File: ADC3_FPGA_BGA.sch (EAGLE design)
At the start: 80 parts, among them CON1 MEZZANINE_2X30, CON2 MEZZANINE_2X30, CON3 USB-SC, IC1 3.3V, IC2 MPM3804, IC3 1.0V, IC4 LFD2NX-40, IC5 EEPROM, IC6 93LC56, IC7 FT2232H, IC8 HyperRAM, J1 CLK, X1 25MHz, X2 12MHz

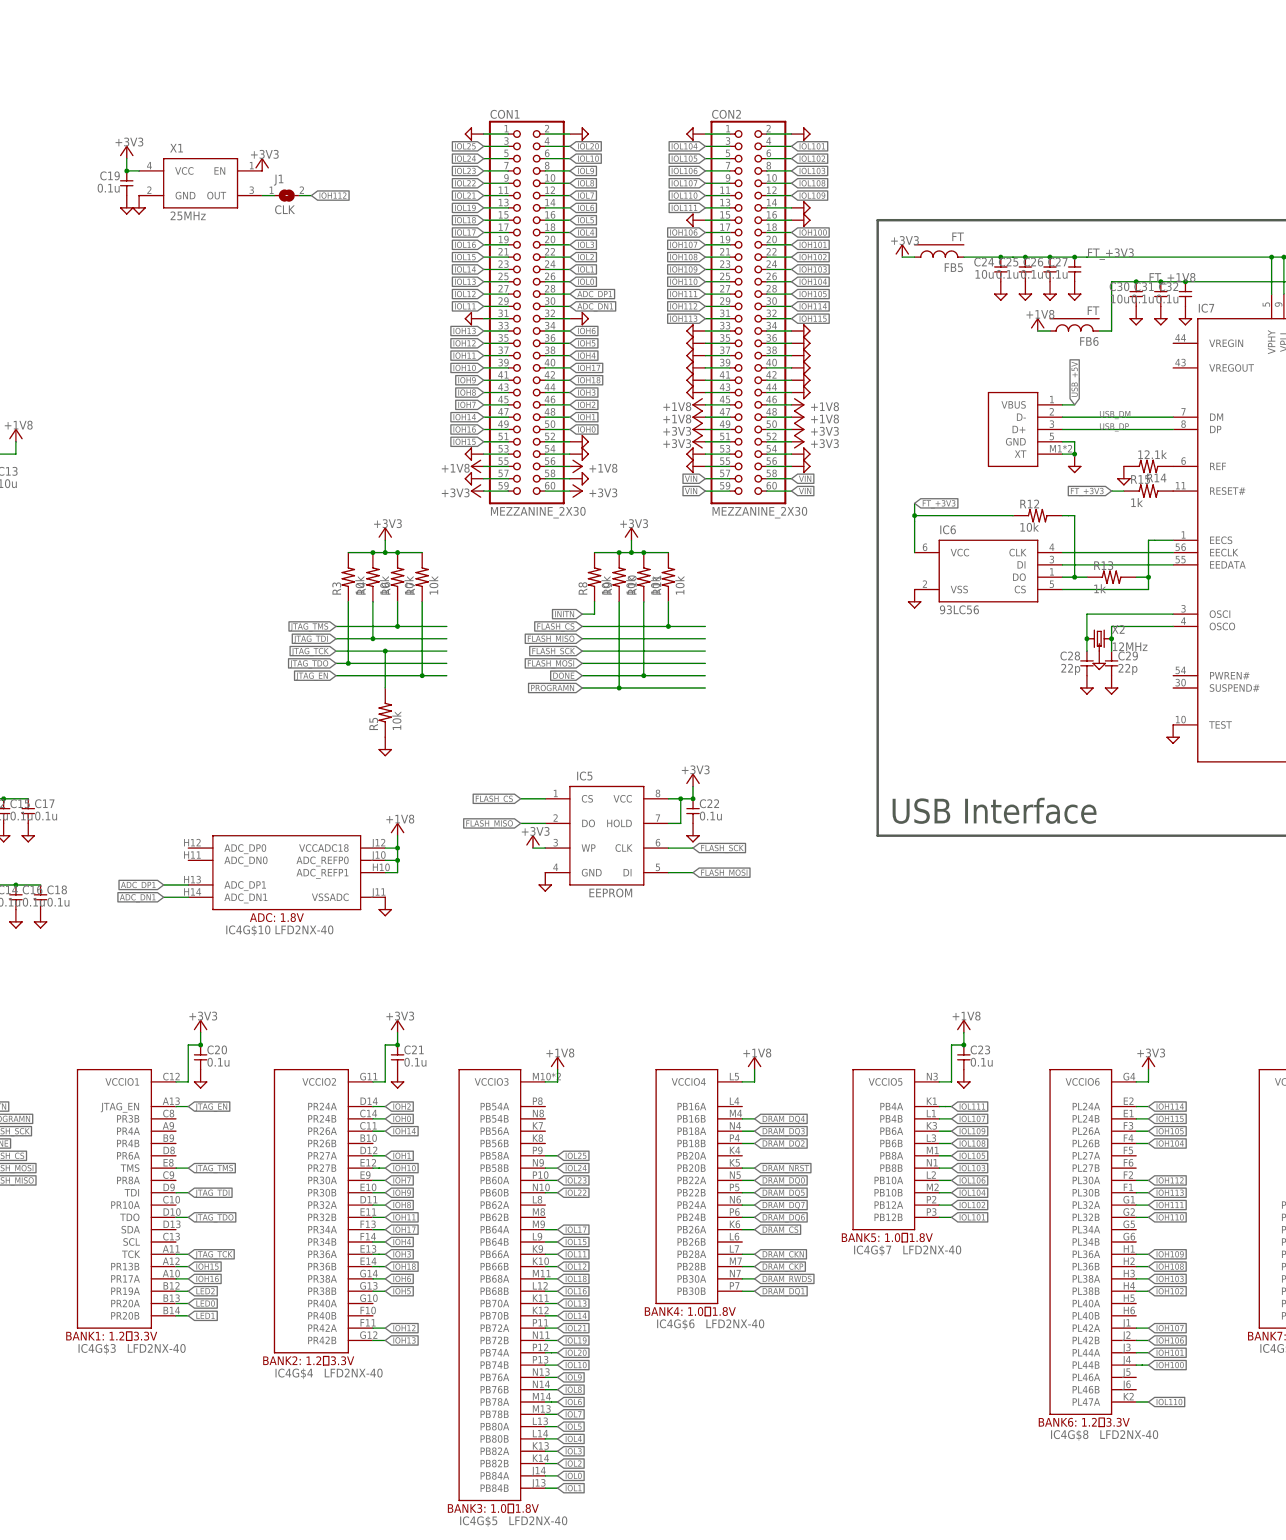
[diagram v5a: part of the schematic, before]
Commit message: コネクタをピン名に変更
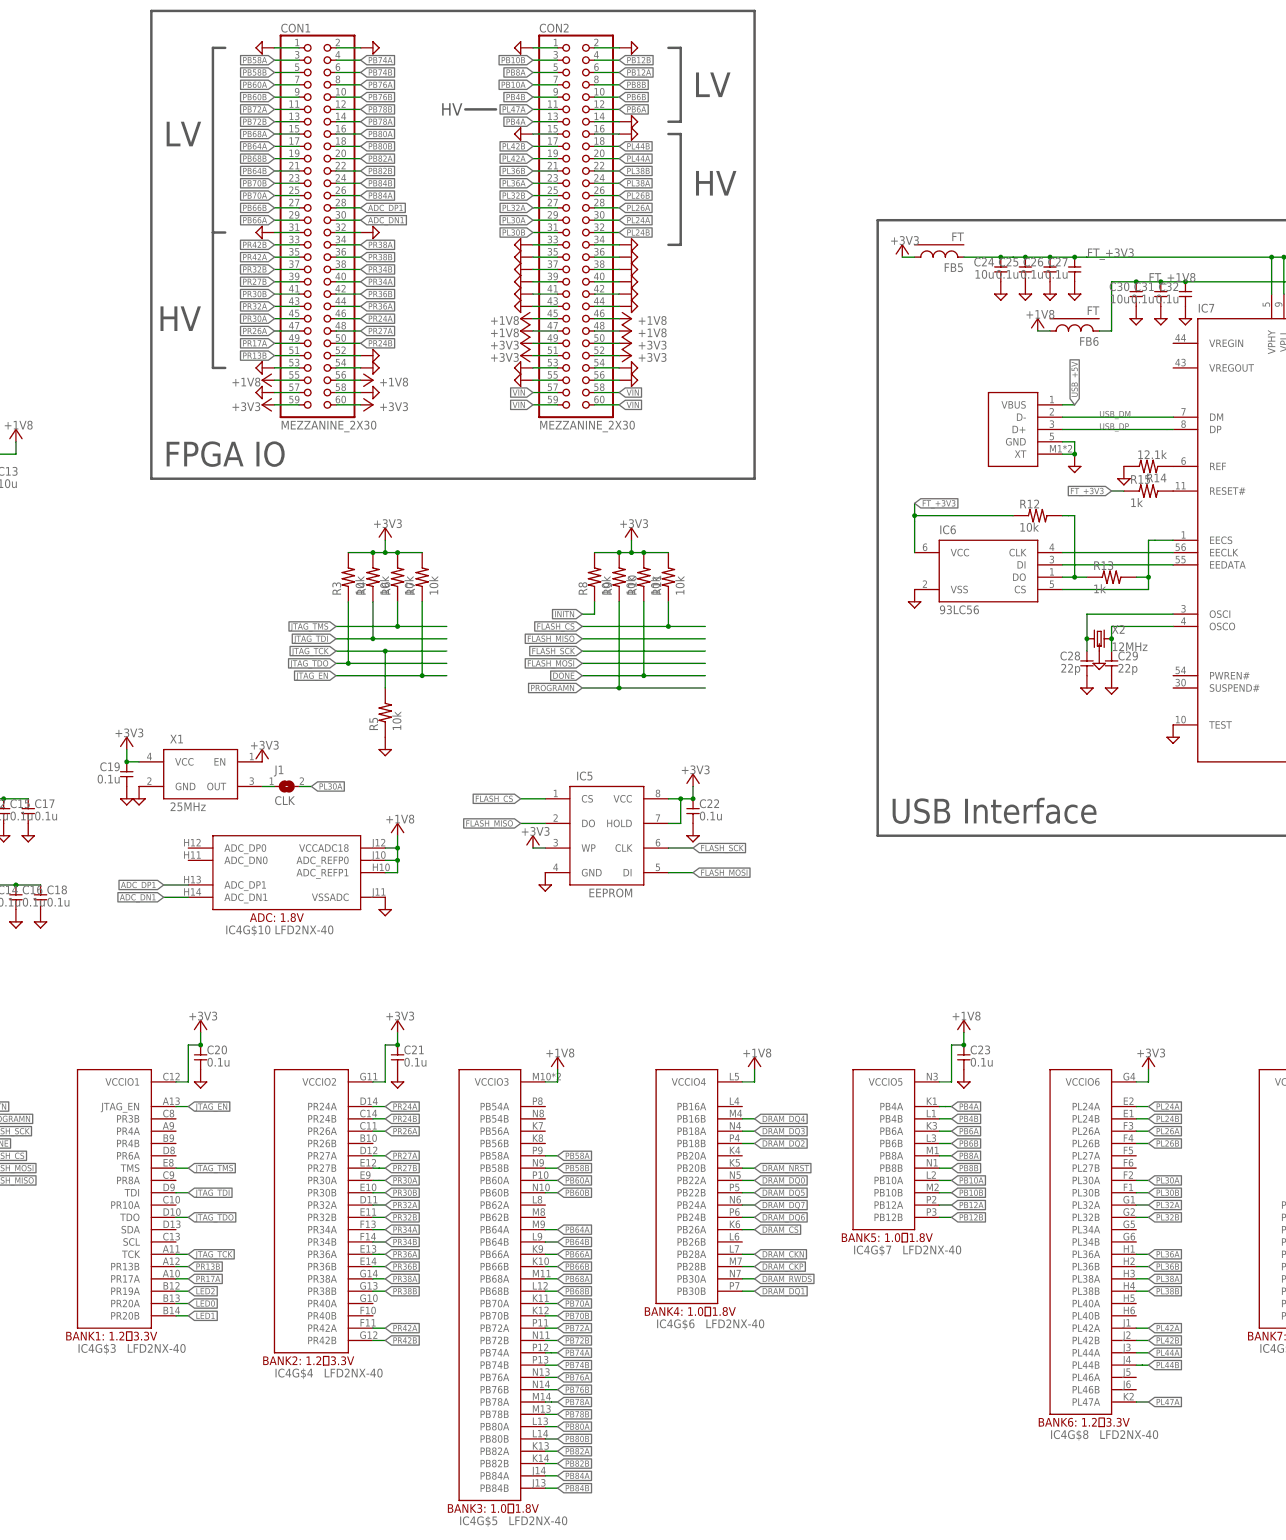
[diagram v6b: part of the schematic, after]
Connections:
- net IOH0 renamed PR24B
- net IOH1 renamed PR27A
- net IOH10 renamed PR27B
- net IOH100 renamed PL44B
- net IOH101 renamed PL44A
- net IOH102 renamed PL38B
- net IOH103 renamed PL38A
- net IOH104 renamed PL26B
- net IOH105 renamed PL26A
- net IOH106 renamed PL42B
- net IOH107 renamed PL42A
- net IOH108 renamed PL36B
- net IOH109 renamed PL36A
- net IOH11 renamed PR32B
- net IOH110 renamed PL32B
- net IOH111 renamed PL32A
- net IOH112 renamed PL30A
- net IOH113 renamed PL30B
- net IOH114 renamed PL24A
- net IOH115 renamed PL24B
- net IOH12 renamed PR42A
- net IOH13 renamed PR42B
- net IOH14 renamed PR26A
- net IOH15 renamed PR13B
- net IOH16 renamed PR17A
- net IOH17 renamed PR34A
- net IOH18 renamed PR36B
- net IOH2 renamed PR24A
- net IOH3 renamed PR36A
- net IOH4 renamed PR34B
- net IOH5 renamed PR38B
- net IOH6 renamed PR38A
- net IOH7 renamed PR30A
- net IOH8 renamed PR32A
- net IOH9 renamed PR30B
- net IOL0 renamed PB84A
- net IOL1 renamed PB84B
- net IOL10 renamed PB74B
- net IOL101 renamed PB12B
- net IOL102 renamed PB12A
- net IOL103 renamed PB8B
- net IOL104 renamed PB10B
- net IOL105 renamed PB8A
- net IOL106 renamed PB10A
- net IOL107 renamed PB4B
- net IOL108 renamed PB6B
- net IOL109 renamed PB6A
- net IOL11 renamed PB66A
- net IOL110 renamed PL47A
- net IOL111 renamed PB4A
- net IOL12 renamed PB66B
- net IOL13 renamed PB70A
- net IOL14 renamed PB70B
- net IOL15 renamed PB64B
- net IOL16 renamed PB68B
- net IOL17 renamed PB64A
- net IOL18 renamed PB68A
- net IOL19 renamed PB72B
- net IOL2 renamed PB82B
- net IOL20 renamed PB74A
- net IOL21 renamed PB72A
- net IOL22 renamed PB60B
- net IOL23 renamed PB60A
- net IOL24 renamed PB58B
- net IOL25 renamed PB58A
- net IOL3 renamed PB82A
- net IOL4 renamed PB80B
- net IOL5 renamed PB80A
- net IOL6 renamed PB78A
- net IOL7 renamed PB78B
- net IOL8 renamed PB76B
- net IOL9 renamed PB76A
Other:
- note added: "FPGA IO"
- note added: "HV"
- note added: "LV"
- moved on the sheet: C19, CON1, CON2, J1, X1

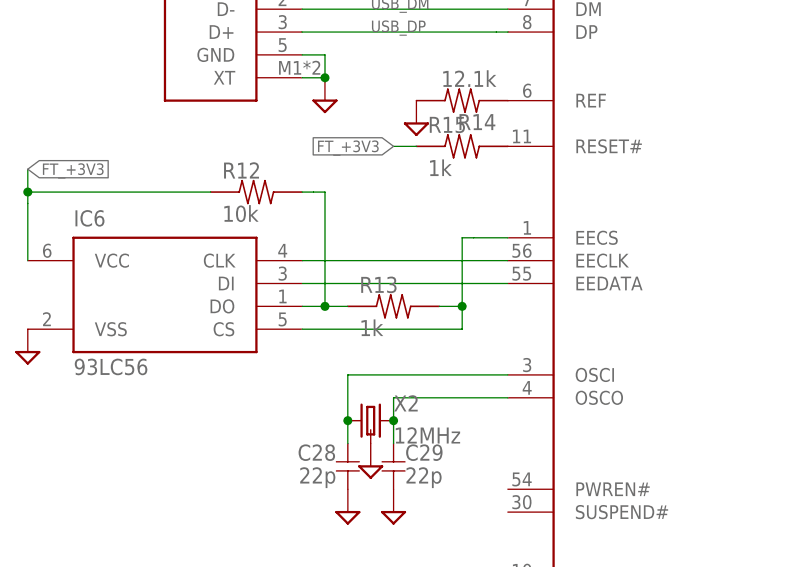
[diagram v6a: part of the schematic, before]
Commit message: FT2232のEEPROMの配線を修正
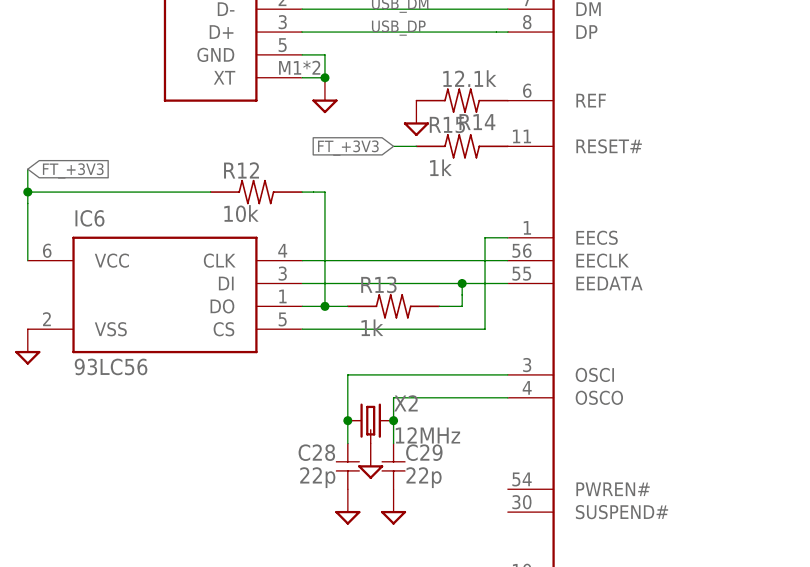
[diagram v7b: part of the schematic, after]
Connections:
- net N$10: now also R13.2
- net N$11: no longer R13.2
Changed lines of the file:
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@@
 <segment>
 <pinref part="IC7" gate="G$1" pin="EEDATA"/>
-<wire x1="269.24" y1="144.78" x2="292.1" y2="144.78" width="0.1524" layer="91"/>
+<wire x1="269.24" y1="144.78" x2="287.02" y2="144.78" width="0.1524" layer="91"/>
 <pinref part="IC6" gate="G$1" pin="DI"/>
+<pinref part="R13" gate="G$1" pin="2"/>
+<wire x1="287.02" y1="144.78" x2="292.1" y2="144.78" width="0.1524" layer="91"/>
+<wire x1="284.48" y1="142.24" x2="287.02" y2="142.24" width="0.1524" layer="91"/>
+<wire x1="287.02" y1="142.24" x2="287.02" y2="143.51" width="0.1524" layer="91"/>
+<wire x1="287.02" y1="143.51" x2="287.02" y2="144.78" width="0.1524" layer="91"/>
+<junction x="287.02" y="144.78"/>
 </segment>
 </net>
@@
 <segment>
 <pinref part="IC7" gate="G$1" pin="EECS"/>
-<wire x1="292.1" y1="149.86" x2="288.29" y2="149.86" width="0.1524" layer="91"/>
-<wire x1="288.29" y1="149.86" x2="287.02" y2="149.86" width="0.1524" layer="91"/>
-<wire x1="287.02" y1="149.86" x2="287.02" y2="142.24" width="0.1524" layer="91"/>
-<wire x1="269.24" y1="139.7" x2="287.02" y2="139.7" width="0.1524" layer="91"/>
-<wire x1="287.02" y1="139.7" x2="287.02" y2="142.24" width="0.1524" layer="91"/>
-<pinref part="R13" gate="G$1" pin="2"/>
-<wire x1="284.48" y1="142.24" x2="287.02" y2="142.24" width="0.1524" layer="91"/>
-<junction x="287.02" y="142.24"/>
+<wire x1="292.1" y1="149.86" x2="289.56" y2="149.86" width="0.1524" layer="91"/>
+<wire x1="289.56" y1="149.86" x2="289.56" y2="139.7" width="0.1524" layer="91"/>
+<wire x1="269.24" y1="139.7" x2="289.56" y2="139.7" width="0.1524" layer="91"/>
 <pinref part="IC6" gate="G$1" pin="CS"/>
 </segment>

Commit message: intel
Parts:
- removed C23: 0.1u, my_rcl:C-1005
- removed J1: CLK, my_rcl:SJ-1608
- removed R10, R11, R7: 10k, my_rcl:R-1608
- removed X1: 25MHz, my_rcl:OSC-KC3225
- added CON4: 8PIN-CON-DIP, my_connector:8PIN-CON-DIP
- added FB8: 2.5V, my_rcl:FB
- added IC9: 2.5V, my_ic:TLV740
- C12, C14, C15, C16, C17, C18, C20: device my_rcl:C-1005 -> my_rcl:C-1608
- C19: value 0.1u -> 10u; device my_rcl:C-1608 -> my_rcl:C-2012
- C21: value 0.1u -> 1u; device my_rcl:C-1005 -> my_rcl:C-1608
- FB3, IC3: value 1.0V -> 1.8V
- FB4: value 1.8V -> 1.2V
- IC4: value LFD2NX-40 -> 10CL016YE144; device my_ic:LFD2NX-40 -> my_ic:10CL016YE144
- IC5: device my_ic:EEPROM_SPI -> my_ic:EEPROM_SPI-WIDE
- IC7: value FT2232H -> FT2232H-2; device my_ic:FT2232H -> my_ic:FT2232H-2
- R2: value 5k -> 10k
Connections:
- net +1V8_DCDC renamed +1V2_DCDC
- net 1.8V_DCDC_SW renamed 1.2V_DCDC_SW
- net N$7 renamed +1V2_FB
- removed net +1V0: C11.1, C12.1, C15.1, C17.1, FB3.2, IC4G$1.VCC, IC4G$1.VCCECLK
- removed net ADC_DN1: CON1.30, IC4G$10.ADC_DN1
- removed net ADC_DP1: CON1.28, IC4G$10.ADC_DP1
- removed net DONE: IC4G$2.DONE, R10.1
- removed net INITN: IC4G$2.INITN, R8.1
- removed net JTAG_EN: IC4G$3.JTAG_EN, R7.1
- removed net N$6: J1.1, X1.OUT
- removed net PB10A: CON2.7, IC4G$7.PB10A
- removed net PB10B: CON2.3, IC4G$7.PB10B
- removed net PB12A: CON2.6, IC4G$7.PB12A
- removed net PB12B: CON2.4, IC4G$7.PB12B
- removed net PB4A: CON2.13, IC4G$7.PB4A
- removed net PB4B: CON2.9, IC4G$7.PB4B
- removed net PB58A: CON1.3, IC4G$5.PB58A
- removed net PB58B: CON1.5, IC4G$5.PB58B
- removed net PB60A: CON1.7, IC4G$5.PB60A
- removed net PB60B: CON1.9, IC4G$5.PB60B
- removed net PB64A: CON1.17, IC4G$5.PB64A
- removed net PB64B: CON1.21, IC4G$5.PB64B
- removed net PB66A: CON1.29, IC4G$5.PB66A
- removed net PB66B: CON1.27, IC4G$5.PB66B
- removed net PB68A: CON1.15, IC4G$5.PB68A
- removed net PB68B: CON1.19, IC4G$5.PB68B
- removed net PB6A: CON2.12, IC4G$7.PB6A
- removed net PB6B: CON2.10, IC4G$7.PB6B
- removed net PB70A: CON1.25, IC4G$5.PB70A
- removed net PB70B: CON1.23, IC4G$5.PB70B
- removed net PB72A: CON1.11, IC4G$5.PB72A
- removed net PB72B: CON1.13, IC4G$5.PB72B
- removed net PB74A: CON1.4, IC4G$5.PB74A
- removed net PB74B: CON1.6, IC4G$5.PB74B
- removed net PB76A: CON1.8, IC4G$5.PB76A
- removed net PB76B: CON1.10, IC4G$5.PB76B
- removed net PB78A: CON1.14, IC4G$5.PB78A
- removed net PB78B: CON1.12, IC4G$5.PB78B
- removed net PB80A: CON1.16, IC4G$5.PB80A
- removed net PB80B: CON1.18, IC4G$5.PB80B
- removed net PB82A: CON1.20, IC4G$5.PB82A
- removed net PB82B: CON1.22, IC4G$5.PB82B
- removed net PB84A: CON1.26, IC4G$5.PB84A
- removed net PB84B: CON1.24, IC4G$5.PB84B
- removed net PB8A: CON2.5, IC4G$7.PB8A
- removed net PB8B: CON2.8, IC4G$7.PB8B
- removed net PL24A: CON2.30, IC4G$8.PL24A
- removed net PL24B: CON2.32, IC4G$8.PL24B
- removed net PL26A: CON2.28, IC4G$8.PL26A
- removed net PL26B: CON2.26, IC4G$8.PL26B
- removed net PL30A: CON2.29, IC4G$8.PL30A, J1.2
- removed net PL30B: CON2.31, IC4G$8.PL30B
- removed net PL32A: CON2.27, IC4G$8.PL32A
- removed net PL32B: CON2.25, IC4G$8.PL32B
- removed net PL36A: CON2.23, IC4G$8.PL36A
- removed net PL36B: CON2.21, IC4G$8.PL36B
- removed net PL38A: CON2.24, IC4G$8.PL38A
- removed net PL38B: CON2.22, IC4G$8.PL38B
- removed net PL42A: CON2.19, IC4G$8.PL42A
- removed net PL42B: CON2.17, IC4G$8.PL42B
- removed net PL44A: CON2.20, IC4G$8.PL44A
- removed net PL44B: CON2.18, IC4G$8.PL44B
- removed net PL47A: CON2.11, IC4G$8.PL47A
- removed net PR13B: CON1.51, IC4G$3.PR13B
- removed net PR17A: CON1.49, IC4G$3.PR17A
- removed net PR24A: CON1.46, IC4G$4.PR24A
- removed net PR24B: CON1.50, IC4G$4.PR24B
- removed net PR26A: CON1.47, IC4G$4.PR26A
- removed net PR27A: CON1.48, IC4G$4.PR27A
- removed net PR27B: CON1.39, IC4G$4.PR27B
- removed net PR30A: CON1.45, IC4G$4.PR30A
- removed net PR30B: CON1.41, IC4G$4.PR30B
- removed net PR32A: CON1.43, IC4G$4.PR32A
- removed net PR32B: CON1.37, IC4G$4.PR32B
- removed net PR34A: CON1.40, IC4G$4.PR34A
- removed net PR34B: CON1.38, IC4G$4.PR34B
- removed net PR36A: CON1.44, IC4G$4.PR36A
- removed net PR36B: CON1.42, IC4G$4.PR36B
- removed net PR38A: CON1.34, IC4G$4.PR38A
- removed net PR38B: CON1.36, IC4G$4.PR38B
- removed net PR42A: CON1.35, IC4G$4.PR42A
- removed net PR42B: CON1.33, IC4G$4.PR42B
- removed net PROGRAMN: IC4G$2.PROG, R9.1
- new net +1V0_LDO1: C21.1, FB8.1, IC9.OUT
- new net +1V2: C13.1, C16.1, C17.1, C18.1, FB4.2, IC4G$1.VCCD_PLL, IC4G$1.VCCINT
- new net +2V5: C12.1, C14.1, C15.1, C19.1, FB8.2, IC4G$1.VCCA
- new net CONFIG: IC4G$2.!CONFIG, IC7.BDBUS7, R3.1
- new net CONF_DONE: IC4G$7.CONF_DONE
- new net IN126/CLK5N: IC4G$8.IN126/CLK8
- new net IN127/CLK5P: IC4G$8.IN127/CLK9
- new net IN128/CLK4N: IC4G$9.IN128/CLK10
- new net IN129/CLK4P: IC4G$9.IN129/CLK11
- new net IN52: IC4G$4.IN52/CLK15
- new net IN53: IC4G$4.IN53/CLK14
- new net IN88/CLK3N: IC4G$6.IN88/CLK7
- new net IN89/CLK3P: IC4G$6.IN89/CLK6
- new net IN90/CLK2N: IC4G$7.IN90/CLK5
- new net IN91/CLK2P: IC4G$7.IN91/CLK4
- new net IO100: IC4G$7.IO100/VREFB6N1
- new net IO101/R16N: IC4G$7.IO101/!CEO
- new net IO103/R16P: IC4G$7.IO103/CLKUSR
- new net IO105: IC4G$7.IO105/VREFB6N0
- new net IO106: IC4G$7.IO106/R2N
- new net IO111: IC4G$8.IO111/VREFB7N0
- new net IO112/CLKOUT2N: IC4G$8.IO112/PLL2_CLKOUT
- new net IO113/CLKOUT2P: IC4G$8.IO113/PLL2_CLKOUT
- new net IO114: IC4G$8.IO114/RUP4
- new net IO115: IC4G$8.IO115/RDN4
- new net IO119: IC4G$8.IO119/VREFB7N1
- new net IO120: IC4G$8.IO120/T23N
- new net IO121: IC4G$8.IO121/T21P
- new net IO125: IC4G$8.IO125T17P
- new net IO132/T12N: IC4G$9.IO132/DATA2
- new net IO133/T12P: IC4G$9.IO133/DATA3
- new net IO134/T11N: IC4G$9.IO134/T11N
- new net IO135/T11P: IC4G$9.IO135/TT1P
- new net IO136: IC4G$9.IO136/VREFB8N0
- new net IO137: IC4G$9.IO137/DATA5
- new net IO141: IC4G$9.IO141/VREFB8N1
- new net IO142: IC4G$9.CDPCLK7
- new net IO143/CLKOUT3N: IC4G$9.IO143/PLL3_CLKOUT
- new net IO144/CLKOUT3P: IC4G$9.IO144/PLL3_CLKOUT
- new net IO49: IC4G$4.IO49
- new net IO50: IC4G$4.IO50/B18P
- new net IO51: IC4G$4.IO51/B18N
- new net IO76: IC4G$6.IO76/RUP3
- new net IO77: IC4G$6.IO77/RDN3
- new net IO80: IC4G$6.IO80/VREFB5N1
- new net IO83: IC4G$6.IO83/VREFB5N0
- new net IO85: IC4G$6.IO85/R22P
- new net IO86/R21N: IC4G$6.IO86/R21N
- new net IO87/R21P: IC4G$6.IO87/R21P
- new net IO98: IC4G$7.IO98/INIT_DONE
- new net IO99: IC4G$7.IO99/CRC_ERROR
- new net STATUS: IC4G$2.!STATUS, R8.1
- net +1V8: now also C11.1, FB3.2, IC4G$5.VCCIO4; no longer C13.1, C14.1, C16.1, C18.1, C23.1, C6.1, CON1.55, CON1.56, CON2.45, CON2.46, CON2.47, CON2.48, FB4.2, IC3.EN, IC3.IN, IC4G$1.VCCAUX, IC4G$1.VCCAUXA, IC4G$1.VCCAUXH3, IC4G$1.VCCAUXH4, IC4G$1.VCCAUXH5, IC4G$10.ADC_REFP0, IC4G$10.ADC_REFP1, IC4G$10.VCCADC18, IC4G$5.VCCIO3, IC4G$6.VCCIO4, IC4G$7.VCCIO5
- net +3V3: now also D2.A, D3.A, D4.A, IC4G$2.VCCIO1, IC4G$3.VCCIO2, IC4G$4.VCCIO3, IC4G$7.VCCIO6, IC4G$8.VCCIO7; no longer C19.1, C20.1, C21.1, CON1.59, CON1.60, CON2.49, CON2.50, CON2.51, CON2.52, IC4G$2.VCCIO0, IC4G$3.VCCIO1, IC4G$4.VCCIO2, IC4G$8.VCCIO6, IC4G$9.VCCIO7, R10.2, R11.2, R7.2, R9.2, X1.EN, X1.VCC
- net DRAM_+1V8: now also R9.2
- net DRAM_CKN: now also IC4G$5.IO71/PLL4_CLKOUT; no longer IC4G$6.PB28A
- net DRAM_CKP: now also IC4G$5.IO72/PLL4_CLKOUT; no longer IC4G$6.PB28B
- net DRAM_CS: now also IC4G$5.IO69/VREFB4N0; no longer IC4G$6.PB26A
- net DRAM_DQ0: now also IC4G$5.IO61/B23P; no longer IC4G$6.PB22A
- net DRAM_DQ1: now also IC4G$5.IO67/RDN2; no longer IC4G$6.PB30B
- net DRAM_DQ2: now also IC4G$5.IO59/B22P; no longer IC4G$6.PB18B
- net DRAM_DQ3: now also IC4G$5.IO58/B21P; no longer IC4G$6.PB18A
- net DRAM_DQ4: now also IC4G$5.IN55/CLK12; no longer IC4G$6.PB16B
- net DRAM_DQ5: now also IC4G$5.IO60/B22N; no longer IC4G$6.PB22B
- net DRAM_DQ6: now also IC4G$5.IO65/VREFB4N1; no longer IC4G$6.PB24B
- net DRAM_DQ7: now also IC4G$5.IO66/RUP2; no longer IC4G$6.PB24A
- net DRAM_NRST: now also R9.1; no longer IC4G$6.PB20B
- net DRAM_RWDS: now also IC4G$5.IO68/B29N; no longer IC4G$6.PB30A
- net FLASH_CS: now also IC4G$2.!CSO, IC7.BDBUS3; no longer IC4G$2.MCSN, R11.1
- net FLASH_MISO: now also IC4G$2.DATA0, IC7.BDBUS2; no longer IC4G$2.MISO
- net FLASH_MOSI: now also IC4G$2.ASDO, IC7.BDBUS1; no longer IC4G$2.MOSI
- net FLASH_SCK: now also IC4G$2.DCLK, IC7.BDBUS0; no longer IC4G$2.MCLK
- net FT_CLK: now also IC4G$2.IN22/CLK0; no longer IC4G$9.PL10A
- net FT_D0: now also IC4G$4.IO46/VREFB3N0; no longer IC4G$9.PL17B
- net FT_D1: now also IC4G$4.IO44/PLL1_CLKOUT; no longer IC4G$9.PL11A
- net FT_D2: now also IC4G$4.IO43/PLL1_CLKOUT; no longer IC4G$9.PL11B
- net FT_D3: now also IC4G$4.IO42/CDPCLK2; no longer IC4G$9.PL17A
- net FT_D4: now also IC4G$4.IO39/VREFB3N1; no longer IC4G$9.PL3B
- net FT_D5: now also IC4G$3.IO33/RDN1; no longer IC4G$9.PL8B
- net FT_D6: now also IC4G$3.IO32/RUP1; no longer IC4G$9.PL3A
- net FT_D7: now also IC4G$3.IO31/VREFB2N1; no longer IC4G$9.PL8A
- net FT_NOE: now also IC4G$2.IO7/VREFB1N0; no longer IC4G$9.PL10B
- net FT_NRD: now also IC4G$3.IO28/VREFB2N0; no longer IC4G$9.PL4A
- net FT_NWR: now also IC4G$2.IO11/VREFB1N1; no longer IC4G$9.PL6B
- net FT_RXNF: now also IC4G$3.IN25/CLK3; no longer IC4G$9.PL4B
- net FT_SIWU: now also IC4G$2.IO10; no longer IC4G$9.PL19A
- net FT_TXNE: now also IC4G$3.IN24/CLK2; no longer IC4G$9.PL6A
- net GND: now also CON4.1, IC4G$2.!CE, IC4G$7.MSEL0, IC4G$7.MSEL1, IC4G$7.MSEL2, IC9.GND; no longer C23.2, CON1.31, CON1.32, CON1.52, CON1.53, CON1.54, CON1.57, CON1.58, CON2.14, CON2.15, CON2.16, CON2.33, CON2.34, CON2.35, CON2.36, CON2.37, CON2.38, CON2.39, CON2.40, CON2.41, CON2.42, CON2.43, CON2.44, CON2.53, CON2.54, CON2.55, CON2.56, IC4G$10.VSSADC, R16.1, R17.1, R18.1, X1.GND
- net JTAG_TCK: now also CON4.5, IC4G$2.TCK; no longer IC4G$3.TCK, IC7.BDBUS0
- net JTAG_TDI: now also CON4.3, IC4G$2.TDI; no longer IC4G$3.TDI, IC7.BDBUS1
- net JTAG_TDO: now also IC4G$2.TDO; no longer IC4G$3.TDO, IC7.BDBUS2, R3.1
- net JTAG_TMS: now also CON4.7, IC4G$2.TMS; no longer IC4G$3.TMS, IC7.BDBUS3
- net LED0: now also R16.1; no longer D2.A, IC4G$3.PR20A
- net LED1: now also R17.1; no longer D3.A, IC4G$3.PR20B
- net LED2: now also R18.1; no longer D4.A, IC4G$3.PR19A
- net VIN: now also CON4.2; no longer CON2.57, CON2.58, CON2.59, CON2.60
- net VIN_DCDC: now also C20.1, C6.1, IC3.EN, IC3.IN, IC9.EN, IC9.IN
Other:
- note removed: "HV"
- note removed: "LV"
- moved on the sheet: C10, C11, C12, C14, C15, C16, C17, C18, C19, C20, C21, C4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
